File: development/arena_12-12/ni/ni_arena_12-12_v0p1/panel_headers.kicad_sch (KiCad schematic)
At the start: 315 parts, among them P1 CONN15, P10 CONN15, P11 CONN15, P12 CONN15, P2 CONN15, P3 CONN15, P4 CONN15, P5 CONN15, P6 CONN15, P7 CONN15, P8 CONN15, P9 CONN15, Q1 MOSFET_NCHAN, U100 74LVC2G17, U101 74LVC2G17, U102 74LVC2G17, U103 74LVC2G17, U104 74LVC2G17, U105 74LVC2G17, U106 74LVC2G17, U107 74LVC2G17, U108 74LVC2G17, U109 74LVC2G17, U110 74LVC2G17, U39 74LVC2G17, U40 74LVC2G17, U41 74LVC2G17, U42 74LVC2G17, U43 74LVC2G17, U44 74LVC2G17, U45 74LVC2G17, U46 74LVC2G17, U47 74LVC2G17, U48 74LVC2G17, U49 74LVC2G17, U50 74LVC2G17, U51 74LVC2G17, U52 74LVC2G17, U53 74LVC2G17, U54 74LVC2G17, U55 74LVC2G17, U56 74LVC2G17, U57 74LVC2G17, U58 74LVC2G17, U59 74LVC2G17, U60 74LVC2G17, U61 74LVC2G17, U62 74LVC2G17, U63 74LVC2G17, U64 74LVC2G17, U65 74LVC2G17, U66 74LVC2G17, U67 74LVC2G17, U68 74LVC2G17, U69 74LVC2G17, U70 74LVC2G17, U71 74LVC2G17, U72 74LVC2G17, U73 74LVC2G17, U74 74LVC2G17, U75 74LVC2G17, U76 74LVC2G17, U77 74LVC2G17, U78 74LVC2G17, U79 74LVC2G17, U80 74LVC2G17, U81 74LVC2G17, U82 74LVC2G17, U83 74LVC2G17, U84 74LVC2G17, U85 74LVC2G17, U86 74LVC2G17, U87 74LVC2G17, U88 74LVC2G17, U89 74LVC2G17, U90 74LVC2G17, U91 74LVC2G17, U92 74LVC2G17, U93 74LVC2G17, U94 74LVC2G17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

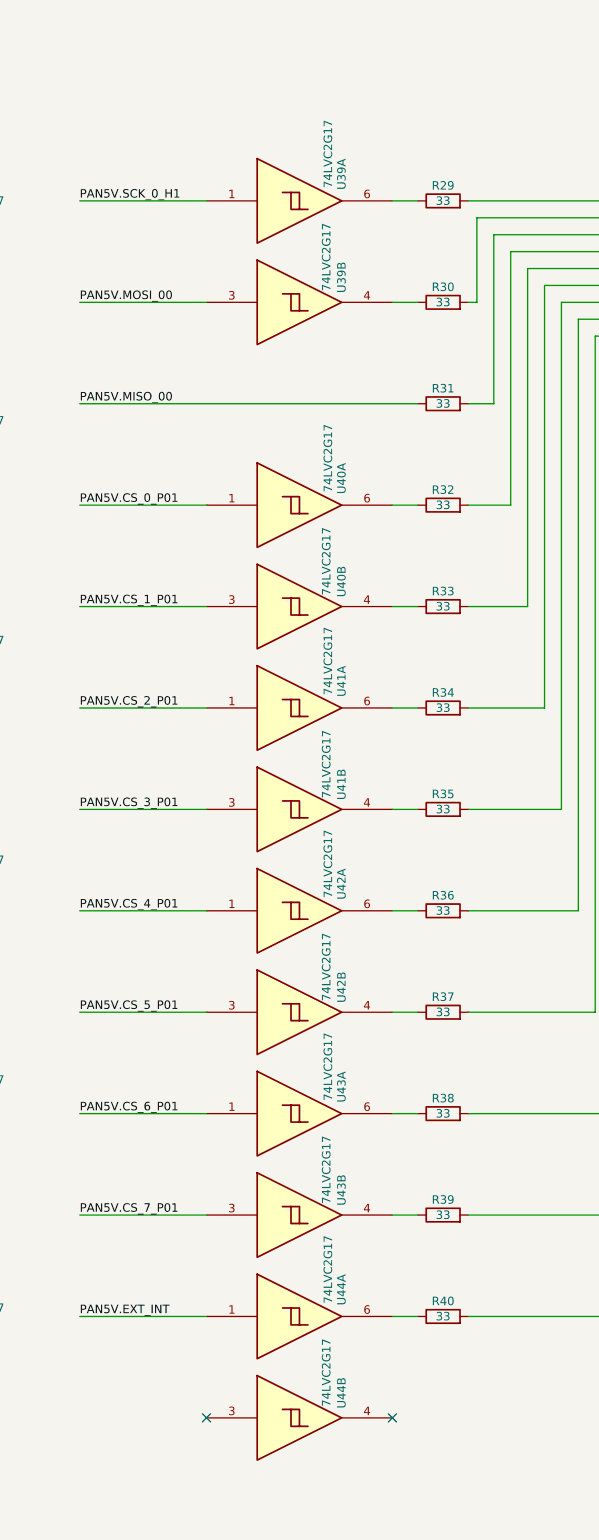
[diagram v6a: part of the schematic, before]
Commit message: Wored on layout for 12-12 NI arena with schmitt buffers.
Worked on layout for schmitt buffers and series term. resitors around
at the base of a panel column.
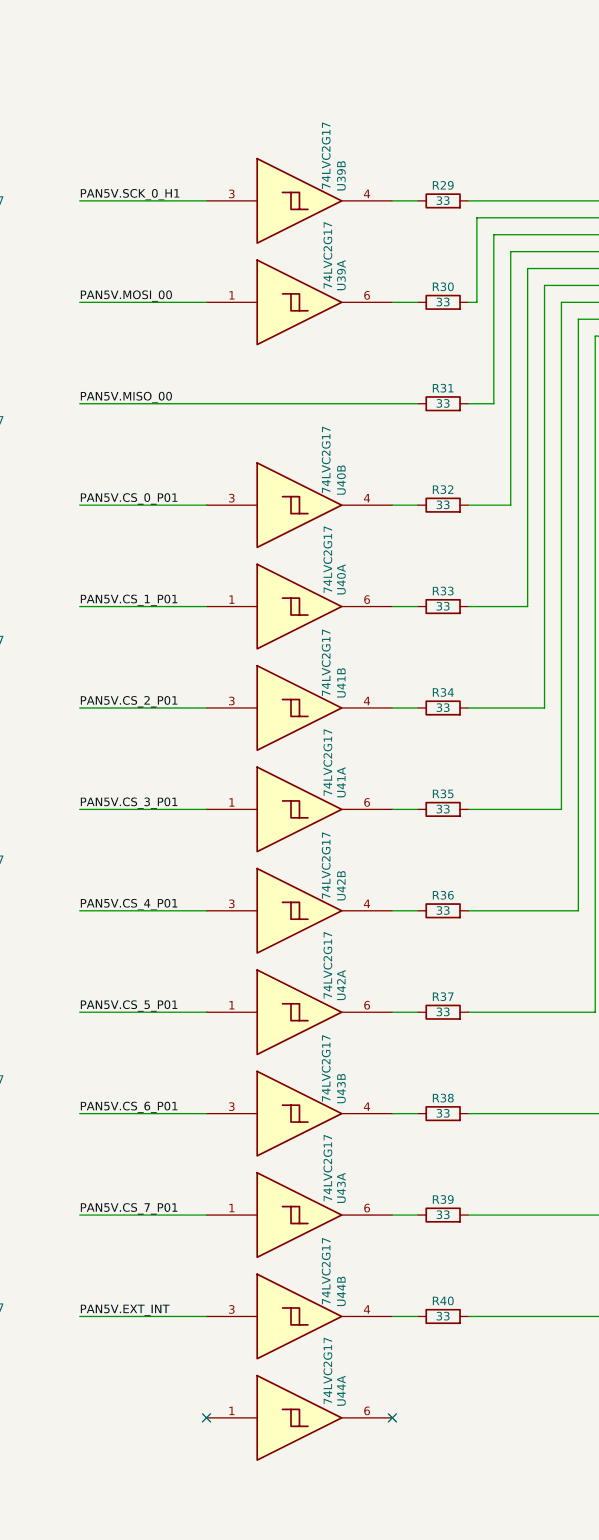
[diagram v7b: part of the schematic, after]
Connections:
- net PAN5V.CS_0_P01: now also U40.3; no longer U40.1
- net PAN5V.CS_1_P01: now also U40.1; no longer U40.3
- net PAN5V.CS_2_P01: now also U41.3; no longer U41.1
- net PAN5V.CS_3_P01: now also U41.1; no longer U41.3
- net PAN5V.CS_4_P01: now also U42.3; no longer U42.1
- net PAN5V.CS_5_P01: now also U42.1; no longer U42.3
- net PAN5V.CS_6_P01: now also U43.3; no longer U43.1
- net PAN5V.CS_7_P01: now also U43.1; no longer U43.3
- net PAN5V.EXT_INT: now also U44.3; no longer U44.1
- net PAN5V.MOSI_00: now also U39.1; no longer U39.3
- net PAN5V.SCK_0_H1: now also U39.3; no longer U39.1
- net at U41.4: now also R34.1; no longer R35.1
- net at U39.4: now also R29.1; no longer R30.1
- net at U43.6: now also R39.1; no longer R38.1
- net at U43.4: now also R38.1; no longer R39.1
- net at U42.6: now also R37.1; no longer R36.1
- net at U40.4: now also R32.1; no longer R33.1
- net at U39.6: now also R30.1; no longer R29.1
- net at U42.4: now also R36.1; no longer R37.1
- net at U41.6: now also R35.1; no longer R34.1
- net at R40.1: now also U44.4; no longer U44.6
- net at U40.6: now also R33.1; no longer R32.1
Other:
- moved on the sheet: U39A, U39B, U40A, U40B, U41A, U41B, U42A, U42B, U43A, U43B, U44A, U44B

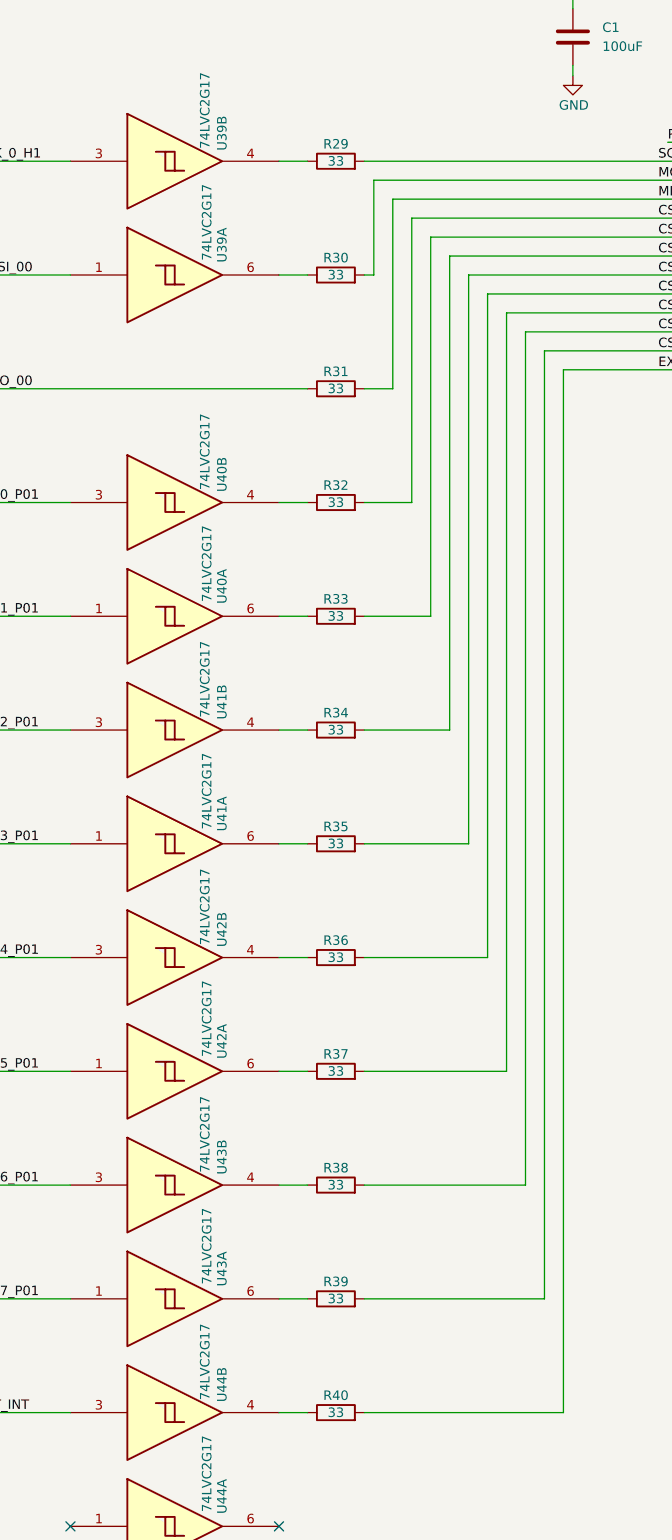
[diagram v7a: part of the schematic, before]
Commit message: Worked on layout for 12-12 ni arena with schmitt buffers.
Finished layout of components at base of panel columns.
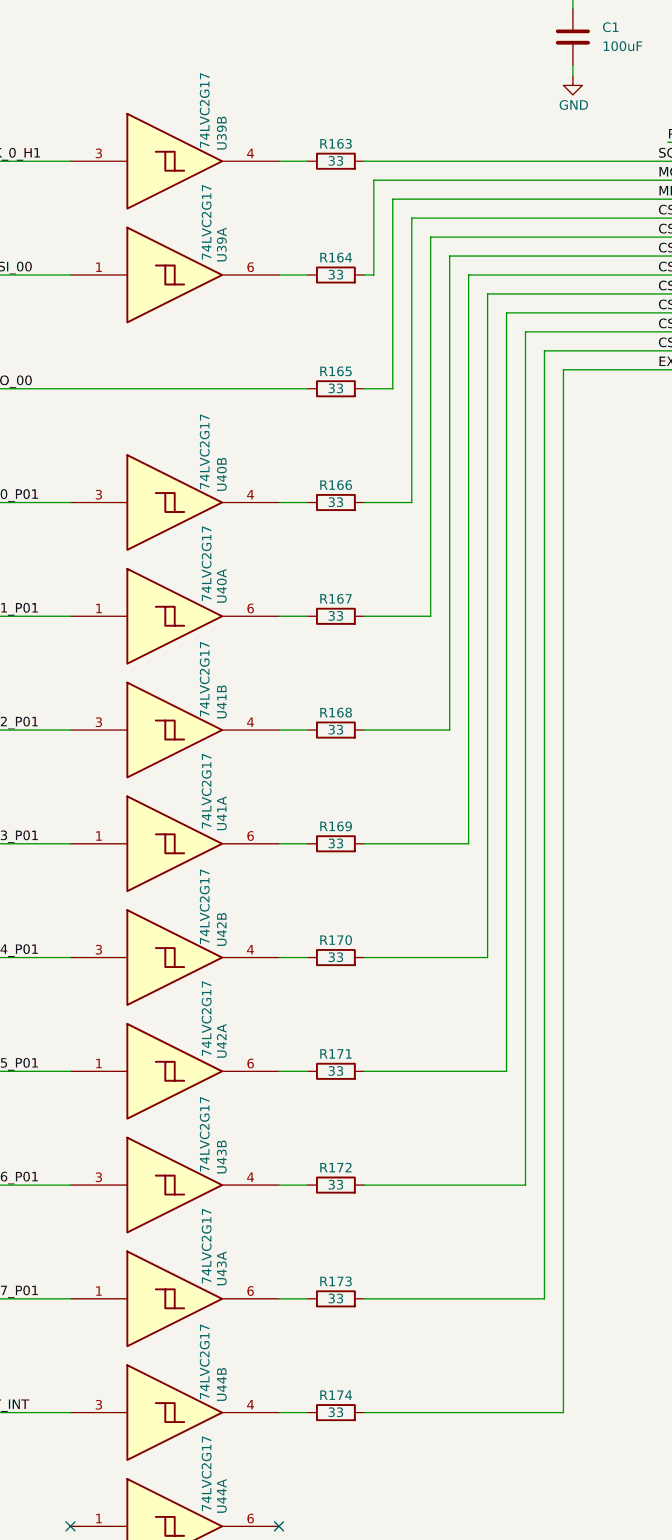
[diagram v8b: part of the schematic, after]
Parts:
- renumbered R29 to R163, R30 to R164, R31 to R165, R32 to R166, R33 to R167, R34 to R168, R35 to R169, R36 to R170, R37 to R171, R38 to R172, R39 to R173, R40 to R174
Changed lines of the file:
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@@
 		(on_board yes)
 		(dnp no)
-		(property "Reference" "R35"
+		(property "Reference" "R169"
 			(at 161.29 162.814 90)
 			(effects
@@
 			(project "ni_arena_12-12"
 				(path "/a2511654-3a17-43f1-8b9e-c45e375533dc/ad9c294f-d898-4a63-8d96-c5c7fb69f139"
-					(reference "R35")
+					(reference "R169")
 					(unit 1)
 				)
@@
 		(on_board yes)
 		(dnp no)
-		(property "Reference" "R30"
+		(property "Reference" "R164"
 			(at 161.29 86.614 90)
 			(effects
@@
 			(project "ni_arena_12-12"
 				(path "/a2511654-3a17-43f1-8b9e-c45e375533dc/ad9c294f-d898-4a63-8d96-c5c7fb69f139"
-					(reference "R30")
+					(reference "R164")
 					(unit 1)
 				)
@@
 		(on_board yes)
 		(dnp no)
-		(property "Reference" "R38"
+		(property "Reference" "R172"
 			(at 161.29 208.534 90)
 			(effects
@@
 			(project "ni_arena_12-12"
 				(path "/a2511654-3a17-43f1-8b9e-c45e375533dc/ad9c294f-d898-4a63-8d96-c5c7fb69f139"
-					(reference "R38")
+					(reference "R172")
 					(unit 1)
 				)
@@
 		(on_board yes)
 		(dnp no)
-		(property "Reference" "R36"
+		(property "Reference" "R170"
 			(at 161.29 178.054 90)
 			(effects
@@
 			(project "ni_arena_12-12"
 				(path "/a2511654-3a17-43f1-8b9e-c45e375533dc/ad9c294f-d898-4a63-8d96-c5c7fb69f139"
-					(reference "R36")
+					(reference "R170")
 					(unit 1)
 				)
@@
 		(on_board yes)
 		(dnp no)
-		(property "Reference" "R31"
+		(property "Reference" "R165"
 			(at 161.29 101.854 90)
 			(effects
@@
 			(project "ni_arena_12-12"
 				(path "/a2511654-3a17-43f1-8b9e-c45e375533dc/ad9c294f-d898-4a63-8d96-c5c7fb69f139"
-					(reference "R31")
+					(reference "R165")
 					(unit 1)
 				)
@@
 		(on_board yes)
 		(dnp no)
-		(property "Reference" "R29"
+		(property "Reference" "R163"
 			(at 161.29 71.374 90)
 			(effects
@@
 			(project "ni_arena_12-12"
 				(path "/a2511654-3a17-43f1-8b9e-c45e375533dc/ad9c294f-d898-4a63-8d96-c5c7fb69f139"
-					(reference "R29")
+					(reference "R163")
 					(unit 1)
 				)
@@
 		(on_board yes)
 		(dnp no)
-		(property "Reference" "R39"
+		(property "Reference" "R173"
 			(at 161.29 223.774 90)
 			(effects
@@
 			(project "ni_arena_12-12"
 				(path "/a2511654-3a17-43f1-8b9e-c45e375533dc/ad9c294f-d898-4a63-8d96-c5c7fb69f139"
-					(reference "R39")
+					(reference "R173")
 					(unit 1)
 				)
@@
 		(on_board yes)
 		(dnp no)
-		(property "Reference" "R40"
+		(property "Reference" "R174"
 			(at 161.29 239.014 90)
 			(effects
@@
 			(project "ni_arena_12-12"
 				(path "/a2511654-3a17-43f1-8b9e-c45e375533dc/ad9c294f-d898-4a63-8d96-c5c7fb69f139"
-					(reference "R40")
+					(reference "R174")
 					(unit 1)
 				)
@@
 		(on_board yes)
 		(dnp no)
-		(property "Reference" "R37"
+		(property "Reference" "R171"
 			(at 161.29 193.294 90)
 			(effects
@@
 			(project "ni_arena_12-12"
 				(path "/a2511654-3a17-43f1-8b9e-c45e375533dc/ad9c294f-d898-4a63-8d96-c5c7fb69f139"
-					(reference "R37")
+					(reference "R171")
 					(unit 1)
 				)
@@
 		(on_board yes)
 		(dnp no)
-		(property "Reference" "R34"
+		(property "Reference" "R168"
 			(at 161.29 147.574 90)
 			(effects
@@
 			(project "ni_arena_12-12"
 				(path "/a2511654-3a17-43f1-8b9e-c45e375533dc/ad9c294f-d898-4a63-8d96-c5c7fb69f139"
-					(reference "R34")
+					(reference "R168")
 					(unit 1)
 				)
@@
 		(on_board yes)
 		(dnp no)
-		(property "Reference" "R32"
+		(property "Reference" "R166"
 			(at 161.29 117.094 90)
 			(effects
@@
 			(project "ni_arena_12-12"
 				(path "/a2511654-3a17-43f1-8b9e-c45e375533dc/ad9c294f-d898-4a63-8d96-c5c7fb69f139"
-					(reference "R32")
+					(reference "R166")
 					(unit 1)
 				)
@@
 		(on_board yes)
 		(dnp no)
-		(property "Reference" "R33"
+		(property "Reference" "R167"
 			(at 161.29 132.334 90)
 			(effects
@@
 			(project "ni_arena_12-12"
 				(path "/a2511654-3a17-43f1-8b9e-c45e375533dc/ad9c294f-d898-4a63-8d96-c5c7fb69f139"
-					(reference "R33")
+					(reference "R167")
 					(unit 1)
 				)
